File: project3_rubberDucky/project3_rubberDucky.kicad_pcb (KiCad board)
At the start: 2 copper layers, 15.8 x 50.4 mm, 14 parts, among them J2 Conn_02x07_Odd_Even, J3 Micro_SD_Card, U1 MCP1700-3302E_SOT23, U2 AT32UC3B1512, U3 USB_A_Cust

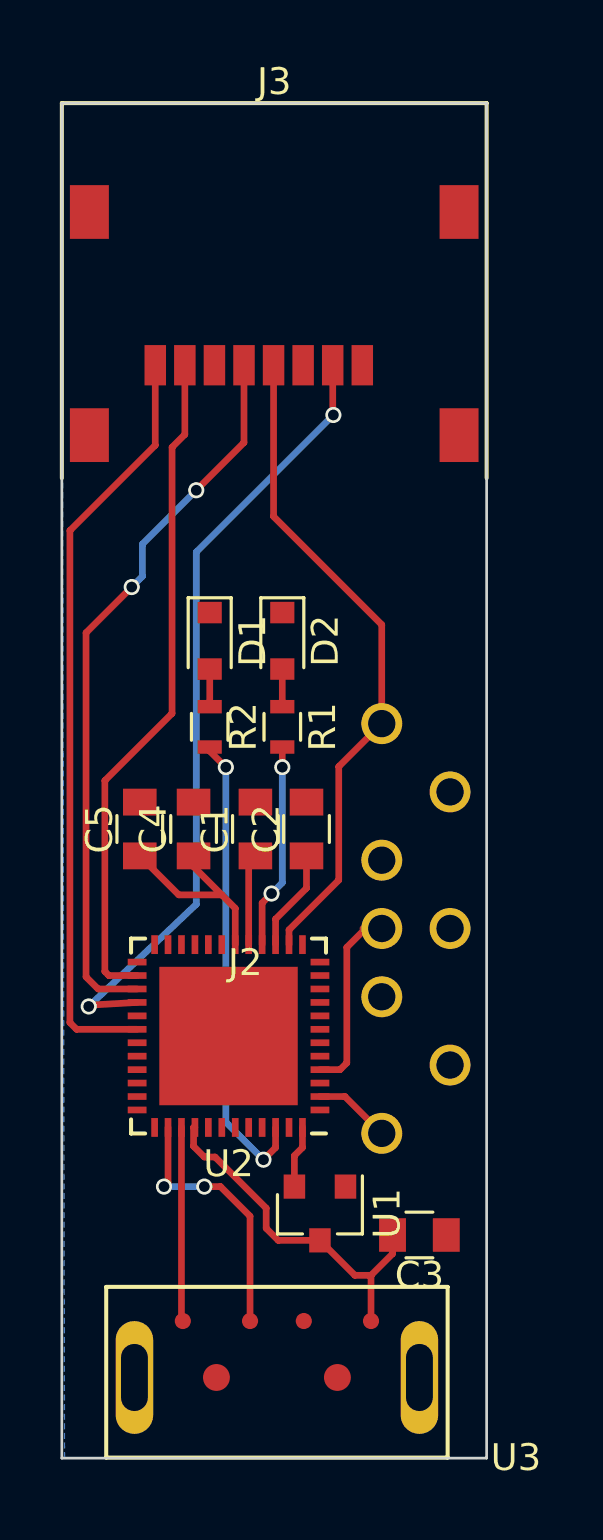
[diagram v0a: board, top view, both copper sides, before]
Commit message: Fixing issues brad found
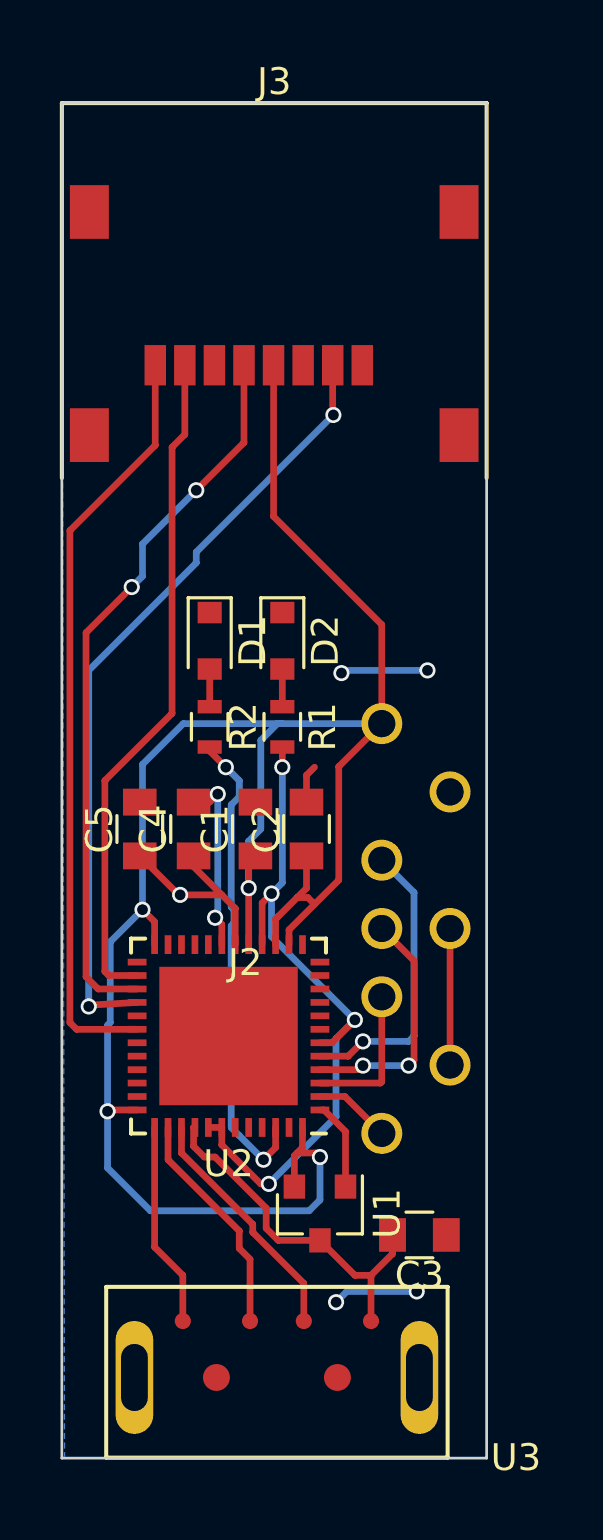
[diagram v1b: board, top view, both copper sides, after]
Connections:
- U3 pad 2: GND -> Net-(U2-Pad39)
- U3 pad 4: Net-(U2-Pad39) -> GND
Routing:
- net /3V3: track 34.6 -> 81.2 mm, vias 0 -> 4
- net GND: track 0.00 -> 31.2 mm, vias 0 -> 6
- net /1V8: track 15.3 -> 33.9 mm, vias 2 -> 5
- net Net-(J2-Pad5): track 0.00 -> 10.8 mm, vias 0 -> 1
- net Net-(J2-Pad9): track 0.00 -> 5.48 mm
- net Net-(U2-Pad39): track 7.22 -> 9.08 mm
- net Net-(U2-Pad38): track 9.82 -> 8.46 mm, vias 2 -> 0
- net Net-(J2-Pad7): track 7.69 -> 9.04 mm, vias 0 -> 2
- net Net-(R1-Pad2): track 17.6 -> 18.2 mm

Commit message: moved edge and fixed ground net
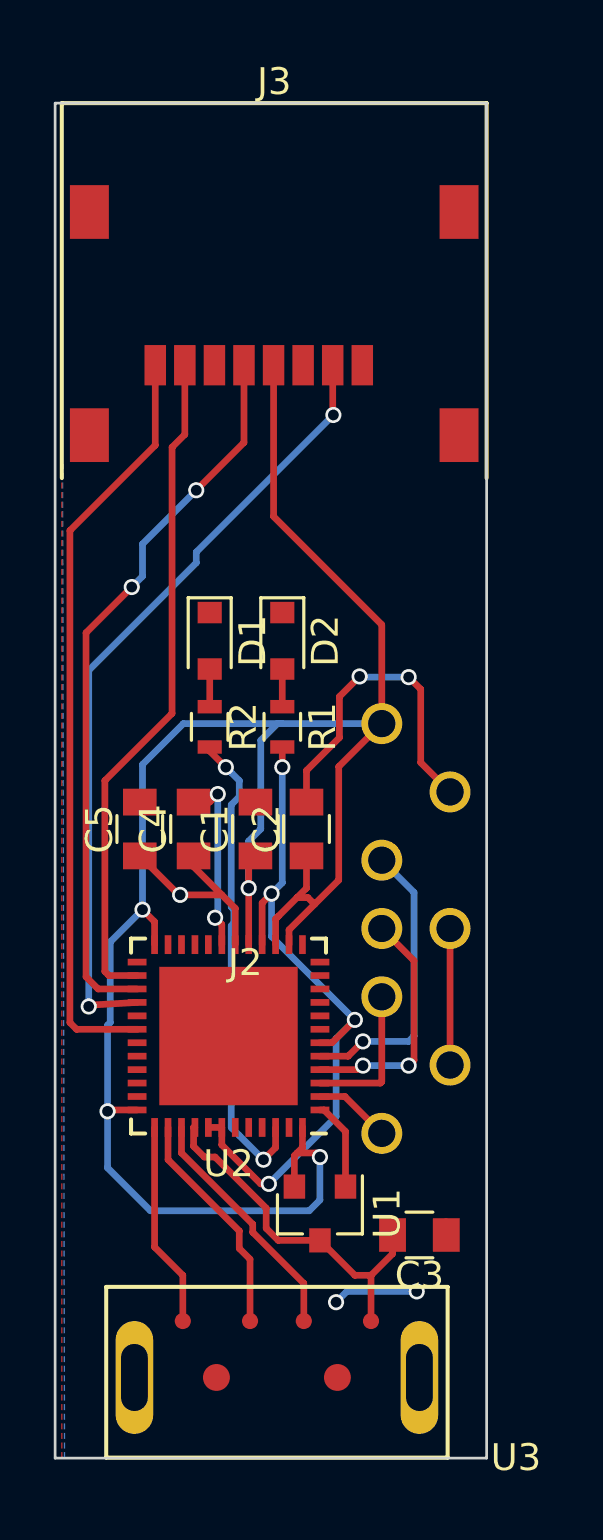
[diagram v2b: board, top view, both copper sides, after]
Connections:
- U3 pad 5: (no net) -> GND
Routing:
- net GND: track 31.2 -> 35.6 mm, vias 6 -> 4
- net (no net): track 0.00 -> 3.17 mm, vias 0 -> 2
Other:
- board size 15.8 x 50.4 mm -> 16 x 50.4 mm
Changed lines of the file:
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@@
 (kicad_pcb (version 4) (host pcbnew 4.0.7-e2-6376~58~ubuntu16.04.1)
   (general
-    (links 52)
+    (links 56)
     (no_connects 0)
-    (area 151.467618 83.525 171.39 136.755)
+    (area 152.999999 85.249999 169.150001 135.750001)
     (thickness 1.6)
     (drawings 4)
-    (tracks 204)
+    (tracks 209)
     (zones 0)
     (modules 14)
@@
     (pad 4 smd circle (at -3.5 0) (size 0.6 0.6) (layers F.Cu F.Paste F.Mask)
       (net 2 GND))
-    (pad 5 thru_hole oval (at 5.3 2.1) (size 1.4 4.2) (drill oval 1 2.5) (layers *.Cu *.Mask))
-    (pad 5 thru_hole oval (at -5.3 2.1) (size 1.4 4.2) (drill oval 1 2.5) (layers *.Cu *.Mask))
-    (pad 5 smd circle (at 2.25 2.1) (size 1 1) (layers F.Cu F.Paste F.Mask))
-    (pad 5 smd circle (at -2.25 2.1) (size 1 1) (layers F.Cu F.Paste F.Mask))
-  )
-  (gr_line (start 169.1 85.3) (end 153.3 85.3) (angle 90) (layer Edge.Cuts) (width 0.1))
-  (gr_line (start 169.1 135.7) (end 153.3 135.7) (angle 90) (layer Edge.Cuts) (width 0.1))
-  (gr_line (start 153.3 85.3) (end 153.3 135.7) (angle 90) (layer Edge.Cuts) (width 0.1))
+    (pad 5 thru_hole oval (at 5.3 2.1) (size 1.4 4.2) (drill oval 1 2.5) (layers *.Cu *.Mask)
+      (net 2 GND))
+    (pad 5 thru_hole oval (at -5.3 2.1) (size 1.4 4.2) (drill oval 1 2.5) (layers *.Cu *.Mask)
+      (net 2 GND))
+    (pad 5 smd circle (at 2.25 2.1) (size 1 1) (layers F.Cu F.Paste F.Mask)
+      (net 2 GND))
+    (pad 5 smd circle (at -2.25 2.1) (size 1 1) (layers F.Cu F.Paste F.Mask)
+      (net 2 GND))
+  )
+  (gr_line (start 169.1 85.3) (end 153.05 85.3) (angle 90) (layer Edge.Cuts) (width 0.1))
+  (gr_line (start 169.1 135.7) (end 153.05 135.7) (angle 90) (layer Edge.Cuts) (width 0.1))
+  (gr_line (start 153.05 85.3) (end 153.05 135.7) (angle 90) (layer Edge.Cuts) (width 0.1))
   (gr_line (start 169.1 85.3) (end 169.1 135.7) (angle 90) (layer Edge.Cuts) (width 0.1))
+  (via (at 163.5 129.9) (size 0.6) (drill 0.4) (layers F.Cu B.Cu) (net 0))
+  (via (at 166.5 129.5) (size 0.6) (drill 0.4) (layers F.Cu B.Cu) (net 0))
+  (segment (start 166.5 129.5) (end 163.9 129.5) (width 0.25) (layer B.Cu) (net 0))
+  (segment (start 163.9 129.5) (end 163.5 129.9) (width 0.25) (layer B.Cu) (net 0))
   (segment (start 162.05 114.85) (end 162.45 114.85) (width 0.25) (layer F.Cu) (net 1))
   (segment (start 162.45 114.85) (end 162.7 115.1) (width 0.25) (layer F.Cu) (net 1))
@@
   (segment (start 160.7 109) (end 161.32 108.38) (width 0.25) (layer B.Cu) (net 1))
   (segment (start 161.32 108.38) (end 161.48 108.38) (width 0.25) (layer B.Cu) (net 1))
-  (segment (start 161.48 108.38) (end 165.2 108.38) (width 0.25) (layer B.Cu) (net 1) (status 800000))
+  (segment (start 161.48 108.38) (end 165.2 108.38) (width 0.25) (layer B.Cu) (net 1))
   (segment (start 155 124.9) (end 155 122.8) (width 0.25) (layer B.Cu) (net 1))
   (segment (start 156.6 126.5) (end 155 124.9) (width 0.25) (layer B.Cu) (net 1))
@@
   (segment (start 161.95 124.45) (end 162.05 124.35) (width 0.25) (layer F.Cu) (net 1))
   (segment (start 162.05 124.35) (end 162.25 124.15) (width 0.25) (layer F.Cu) (net 1))
-  (via (at 163.7 106.5) (size 0.6) (drill 0.4) (layers F.Cu B.Cu) (net 2))
-  (via (at 166.9 106.4) (size 0.6) (drill 0.4) (layers F.Cu B.Cu) (net 2))
-  (segment (start 166.9 106.4) (end 163.8 106.4) (width 0.25) (layer B.Cu) (net 2))
-  (segment (start 163.8 106.4) (end 163.7 106.5) (width 0.25) (layer B.Cu) (net 2))
-  (via (at 163.5 129.9) (size 0.6) (drill 0.4) (layers F.Cu B.Cu) (net 2))
-  (via (at 166.5 129.5) (size 0.6) (drill 0.4) (layers F.Cu B.Cu) (net 2))
-  (segment (start 166.5 129.5) (end 163.9 129.5) (width 0.25) (layer B.Cu) (net 2))
-  (segment (start 163.9 129.5) (end 163.5 129.9) (width 0.25) (layer B.Cu) (net 2))
+  (segment (start 162.4 111.3) (end 162.4 110.125) (width 0.25) (layer F.Cu) (net 2) (status 400000))
+  (segment (start 166.65 109.83) (end 167.74 110.92) (width 0.25) (layer F.Cu) (net 2) (status 800000))
+  (segment (start 166.65 107.1) (end 166.65 109.83) (width 0.25) (layer F.Cu) (net 2))
+  (segment (start 166.2 106.65) (end 166.65 107.1) (width 0.25) (layer F.Cu) (net 2))
+  (via (at 166.2 106.65) (size 0.6) (drill 0.4) (layers F.Cu B.Cu) (net 2))
+  (segment (start 164.4 106.65) (end 166.2 106.65) (width 0.25) (layer B.Cu) (net 2))
+  (segment (start 164.375 106.625) (end 164.4 106.65) (width 0.25) (layer B.Cu) (net 2))
+  (via (at 164.375 106.625) (size 0.6) (drill 0.4) (layers F.Cu B.Cu) (net 2))
+  (segment (start 163.625 107.375) (end 164.375 106.625) (width 0.25) (layer F.Cu) (net 2))
+  (segment (start 163.625 108.9) (end 163.625 107.375) (width 0.25) (layer F.Cu) (net 2))
+  (segment (start 162.4 110.125) (end 163.625 108.9) (width 0.25) (layer F.Cu) (net 2))
   (segment (start 167.74 121.08) (end 167.74 116) (width 0.25) (layer F.Cu) (net 2))
-  (segment (start 162.4 111.3) (end 162.4 110.3) (width 0.25) (layer F.Cu) (net 2))
-  (segment (start 162.4 110.3) (end 162.7 110) (width 0.25) (layer F.Cu) (net 2))
   (segment (start 159.25 116.6) (end 159.25 115.85) (width 0.25) (layer F.Cu) (net 2))
   (segment (start 159.1 111) (end 158.8 111.3) (width 0.25) (layer F.Cu) (net 2))
